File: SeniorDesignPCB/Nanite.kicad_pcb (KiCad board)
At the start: 2 copper layers, 25 parts, among them U1 4017, U2 TLC555

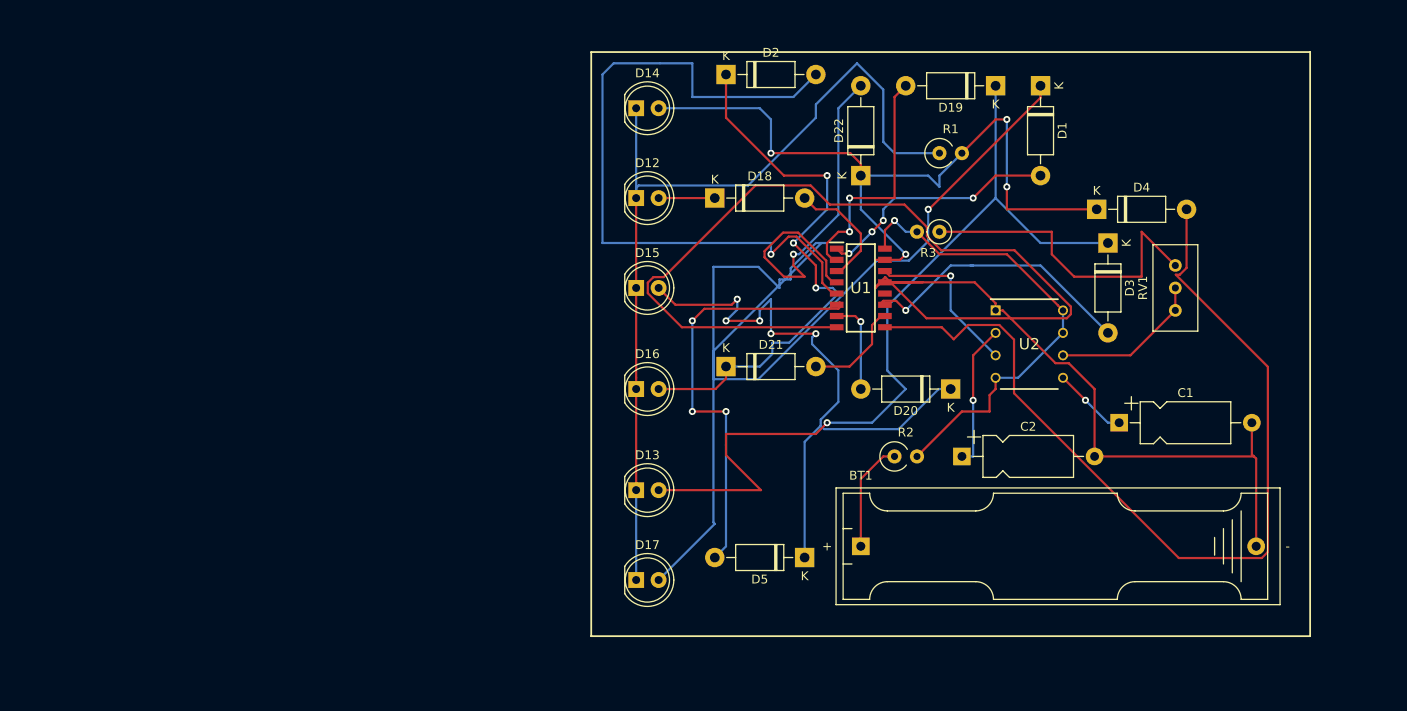
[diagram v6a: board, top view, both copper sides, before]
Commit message: added edge cuts
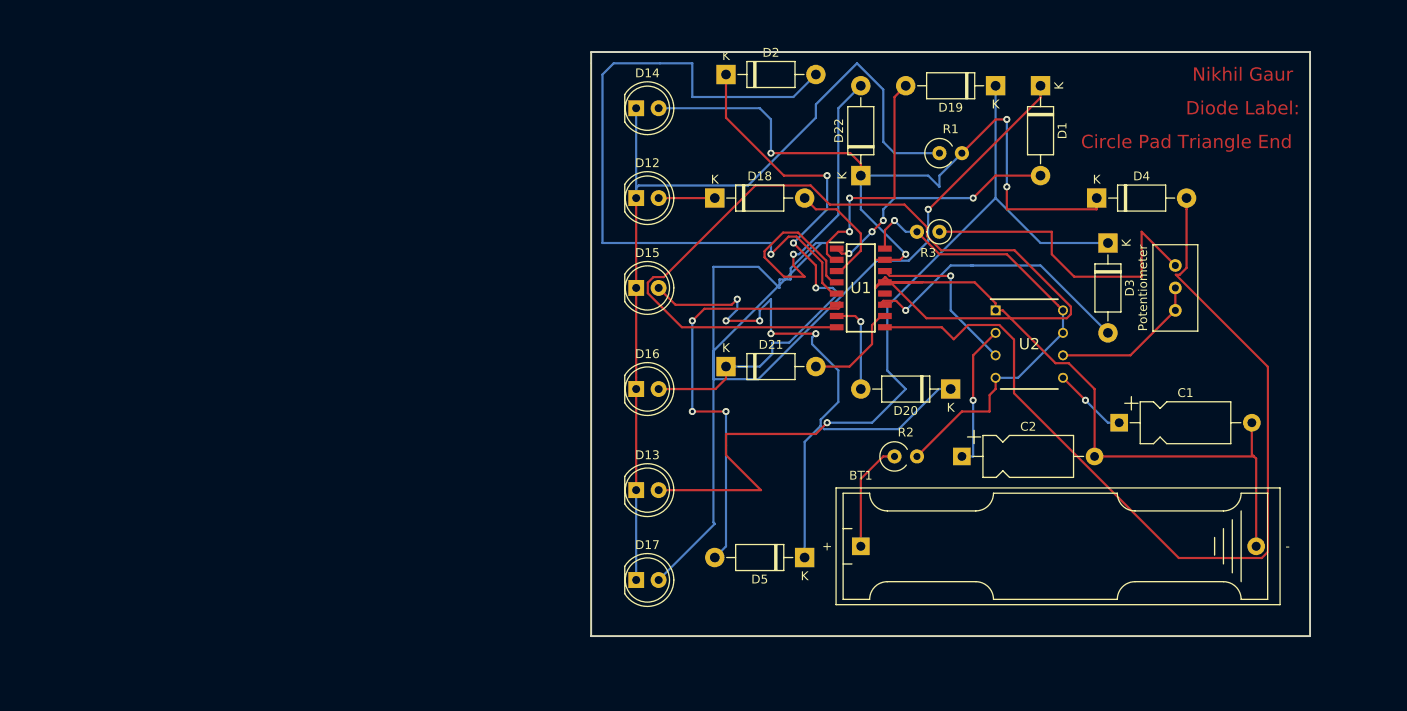
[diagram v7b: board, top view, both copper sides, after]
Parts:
- D1, D18, D19, D2, D20, D21, D22, D3, D4, D5: value 1N4007 -> DIODE
- U2: value TLC555 -> Timer_555
- moved D4 1.27 mm to (144.8, 82.5)
- renumbered RV1 to Potentiometer
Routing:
- net Net-(D4-Pad2): track 103.1 -> 104.4 mm
- net Net-(D14-Pad2): track 84.9 -> 86.2 mm
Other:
- board outline added: 81.3 x 66 mm
- board text added: "Circle Pad Triangle End"
- board text added: "Diode Label:"
- board text added: "Nikhil Gaur"
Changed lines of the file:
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@@
   (general
     (thickness 1.6)
-    (drawings 4)
-    (tracks 322)
+    (drawings 12)
+    (tracks 324)
     (zones 0)
     (modules 25)
@@
       (outputformat 1)
       (mirror false)
-      (drillshape 1)
+      (drillshape 0)
       (scaleselection 1)
-      (outputdirectory ""))
+      (outputdirectory "GerberFiles/"))
   )
   (net 0 "")
@@
   )
   (module Diode_THT:D_DO-41_SOD81_P10.16mm_Horizontal (layer F.Cu)
-    (at 144.78 83.82)
+    (at 144.78 82.55)
     (descr "Diode, DO-41_SOD81 series, Axial, Horizontal, pin pitch=10.16mm, , length*diameter=5.2*2.7mm^2, , http://www.diodes.com/_files/packages/DO-41%20(Plastic).pdf")
     (tags "Diode DO-41_SOD81 series Axial Horizontal pin pitch 10.16mm  length 5.2mm diameter 2.7mm")
@@
       (effects (font (size 1 1) (thickness 0.15)))
     )
-    (fp_text value 1N4007 (at 5.08 2.47) (layer F.Fab)
+    (fp_text value DIODE (at 5.08 2.47) (layer F.Fab)
       (effects (font (size 1 1) (thickness 0.15)))
     )
@@
       (effects (font (size 1 1) (thickness 0.15)))
     )
-    (fp_text value 1N4007 (at 5.08 2.47 270) (layer F.Fab)
+    (fp_text value DIODE (at 5.08 2.47 270) (layer F.Fab)
       (effects (font (size 1 1) (thickness 0.15)))
     )
@@
       (effects (font (size 1 1) (thickness 0.15)))
     )
-    (fp_text value 1N4007 (at 5.08 2.47 180) (layer F.Fab)
+    (fp_text value DIODE (at 5.08 2.47 180) (layer F.Fab)
       (effects (font (size 1 1) (thickness 0.15)))
     )
@@
       (effects (font (size 1 1) (thickness 0.15)))
     )
-    (fp_text value 1N4007 (at 5.08 2.47 270) (layer F.Fab)
+    (fp_text value DIODE (at 5.08 2.47 270) (layer F.Fab)
       (effects (font (size 1 1) (thickness 0.15)))
     )
@@
       (effects (font (size 1 1) (thickness 0.15)))
     )
-    (fp_text value 1N4007 (at 5.08 2.47) (layer F.Fab)
+    (fp_text value DIODE (at 5.08 2.47) (layer F.Fab)
       (effects (font (size 1 1) (thickness 0.15)))
     )
@@
       (effects (font (size 1.27 1.27) (thickness 0.254)))
     )
-    (fp_text value TLC555 (at 0 -6.35) (layer F.SilkS) hide
+    (fp_text value Timer_555 (at 0 -6.35) (layer F.SilkS) hide
       (effects (font (size 1.27 1.27) (thickness 0.254)))
     )
@@
       (effects (font (size 1 1) (thickness 0.15)))
     )
-    (fp_text value "4.7 uF" (at 7.5 3.37) (layer F.Fab)
+    (fp_text value "4.7 uF" (at 3.81 -3.81) (layer F.Fab)
       (effects (font (size 1 1) (thickness 0.15)))
     )
@@
       (effects (font (size 1 1) (thickness 0.15)))
     )
-    (fp_text value "1 nF" (at 7.5 3.37) (layer F.Fab)
+    (fp_text value "1 nF" (at 11.43 -3.81) (layer F.Fab)
       (effects (font (size 1 1) (thickness 0.15)))
     )
@@
       (effects (font (size 1 1) (thickness 0.15)))
     )
-    (fp_text value 1N4007 (at 5.08 2.47 90) (layer F.Fab)
+    (fp_text value DIODE (at 5.08 2.47 90) (layer F.Fab)
       (effects (font (size 1 1) (thickness 0.15)))
     )
@@
       (effects (font (size 1 1) (thickness 0.15)))
     )
-    (fp_text value 1N4007 (at 5.08 2.47) (layer F.Fab)
+    (fp_text value DIODE (at 5.08 2.47) (layer F.Fab)
       (effects (font (size 1 1) (thickness 0.15)))
     )
@@
       (effects (font (size 1 1) (thickness 0.15)))
     )
-    (fp_text value 1N4007 (at 5.08 2.47 180) (layer F.Fab)
+    (fp_text value DIODE (at 5.08 2.47 180) (layer F.Fab)
       (effects (font (size 1 1) (thickness 0.15)))
     )
@@
       (effects (font (size 1 1) (thickness 0.15)))
     )
-    (fp_text value 1N4007 (at 5.08 2.47 180) (layer F.Fab)
+    (fp_text value DIODE (at 5.08 2.47 180) (layer F.Fab)
       (effects (font (size 1 1) (thickness 0.15)))
     )
@@
       (effects (font (size 1 1) (thickness 0.15)))
     )
-    (fp_text value 1N4007 (at 5.08 2.47) (layer F.Fab)
+    (fp_text value DIODE (at 5.08 2.47) (layer F.Fab)
       (effects (font (size 1 1) (thickness 0.15)))
     )
@@
     (descr "Potentiometer, vertical, Bourns 3296W, https://www.bourns.com/pdfs/3296.pdf")
     (tags "Potentiometer vertical Bourns 3296W")
-    (fp_text reference RV1 (at -2.54 -3.66 90) (layer F.SilkS)
+    (fp_text reference Potentiometer (at -2.54 -3.66 90) (layer F.SilkS)
       (effects (font (size 1 1) (thickness 0.15)))
     )
@@
       (effects (font (size 1 1) (thickness 0.15)))
     )
-    (fp_text value 100k (at 1.27 2.37 180) (layer F.Fab)
+    (fp_text value 100k (at -1.27 2.37 180) (layer F.Fab)
       (effects (font (size 1 1) (thickness 0.15)))
     )
@@
       (effects (font (size 1 1) (thickness 0.15)))
     )
-    (fp_text value 4.7k (at 1.27 2.72) (layer F.Fab)
+    (fp_text value 4.7k (at -3.81 0) (layer F.Fab)
       (effects (font (size 1 1) (thickness 0.15)))
     )
@@
       (rotate (xyz 0 0 0))
     )
+  )
+  (gr_line (start 87.63 67.31) (end 87.63 66.04) (layer Edge.Cuts) (width 0.15))
+  (gr_line (start 87.63 132.08) (end 87.63 67.31) (layer Edge.Cuts) (width 0.15))
+  (gr_line (start 168.91 132.08) (end 87.63 132.08) (layer Edge.Cuts) (width 0.15))
+  (gr_line (start 168.91 66.04) (end 168.91 132.08) (layer Edge.Cuts) (width 0.15))
+  (gr_line (start 87.63 66.04) (end 168.91 66.04) (layer Edge.Cuts) (width 0.15))
+  (gr_text "Circle Pad Triangle End" (at 154.94 76.2) (layer F.Cu)
+    (effects (font (size 1.5 1.5) (thickness 0.3)))
+  )
+  (gr_text "Diode Label:" (at 161.29 72.39) (layer F.Cu)
+    (effects (font (size 1.5 1.5) (thickness 0.3)))
+  )
+  (gr_text "Nikhil Gaur\n" (at 161.29 68.58) (layer F.Cu)
+    (effects (font (size 1.5 1.5) (thickness 0.3)))
   )
   (gr_line (start 87.63 66.04) (end 168.91 66.04) (layer F.SilkS) (width 0.2))
@@
   (segment (start 133.35 73.66) (end 129.54 77.47) (width 0.25) (layer F.Cu) (net 3))
   (segment (start 134.62 73.66) (end 133.35 73.66) (width 0.25) (layer F.Cu) (net 3))
+  (segment (start 144.78 83.82) (end 144.78 82.55) (width 0.25) (layer F.Cu) (net 3))
   (segment (start 92.71 82.55) (end 92.71 102.87) (width 0.25) (layer F.Cu) (net 4))
   (segment (start 92.71 102.87) (end 92.71 115.57) (width 0.25) (layer F.Cu) (net 4))
@@
   (segment (start 113.03 109.22) (end 114.3 107.95) (width 0.25) (layer F.Cu) (net 9))
   (segment (start 121.10001 94.79999) (end 121.10001 96.97001) (width 0.25) (layer B.Cu) (net 9))
-  (segment (start 120.835 94.615) (end 121.26 94.615) (width 0.25) (layer F.Cu) (net 25))
   (segment (start 138.43 87.63) (end 146.05 87.63) (width 0.25) (layer B.Cu) (net 9))
   (segment (start 133.35 82.55) (end 138.43 87.63) (width 0.25) (layer B.Cu) (net 9))
@@
   (segment (start 100.42499 95.06501) (end 115.5714 95.06501) (width 0.25) (layer F.Cu) (net 24))
   (segment (start 99.06 96.43) (end 100.42499 95.06501) (width 0.25) (layer F.Cu) (net 24))
+  (segment (start 120.835 94.615) (end 121.26 94.615) (width 0.25) (layer F.Cu) (net 25))
   (segment (start 146.05 97.79) (end 138.43 90.17) (width 0.25) (layer B.Cu) (net 25))
   (via (at 123.19 95.25) (size 0.8) (drill 0.4) (layers F.Cu B.Cu) (net 25))
@@
   (segment (start 127.258 97.155) (end 128.618001 98.515001) (width 0.25) (layer F.Cu) (net 26))
   (segment (start 120.835 97.155) (end 127.258 97.155) (width 0.25) (layer F.Cu) (net 26))
+  (segment (start 154.94 83.82) (end 154.94 82.55) (width 0.25) (layer F.Cu) (net 26))
 )
